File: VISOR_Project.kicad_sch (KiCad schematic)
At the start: 28 parts, among them U1 OPA170AIDBVR, U3 DRV8871DDA, U4 GD32VF103R, U5 MCP6002-xP, U6 MCP6002-xP

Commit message: project name
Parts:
- removed C5, C7: 100uF Keramisk, symbol Device:C_Small
- removed C6, C8: C_Polarized 4.7uF, symbol Device:C_Polarized
- removed NT1: NetTie_2, symbol Device:NetTie_2
- removed R10: 100Ω, symbol Device:R
- removed R7: 10kΩ, symbol Device:R
- removed R8: 5.1kΩ, symbol Device:R
- removed U5: MCP6002-xP, symbol Amplifier_Operational:MCP6002-xP
- removed unit 3 of U6
- added C1: 0.1uF, symbol Device:C
- added C2: 1uF, symbol Device:C
- added LD1: PL520, OptoDevice:LaserDiode_TO38ICut-3, symbol Diode_Laser:PL520
- added R1: 65Ω, symbol Device:R
- added R2: 390Ω, symbol Device:R
- added U2: LM317_TO-220, Package_TO_SOT_THT:TO-220-3_Vertical, symbol Regulator_Linear:LM317_TO-220
- added V1: 12, symbol Simulation_SPICE:VDC
- renumbered Ci to Ci1, R(SH) to R(SH)1
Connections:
- net at Ci1.1, R(SH)1.2: now also D1.2 (A); no longer D1.1 (K)
- net at C1.1, Ci1.2, R(SH)1.1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: now also D1.1 (K); no longer D1.2 (A)
- new net: C2.2, LD1.1 (A), R1.2, U2.2 (VO)
- new net: C1.1, C2.1, LD1.3 (C), R2.1, V1.2
- new net: C1.2, U2.3 (VI), V1.1
- new net: R1.1, R2.2, U2.1 (ADJ)
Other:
- moved on the sheet: D1, R5, R6

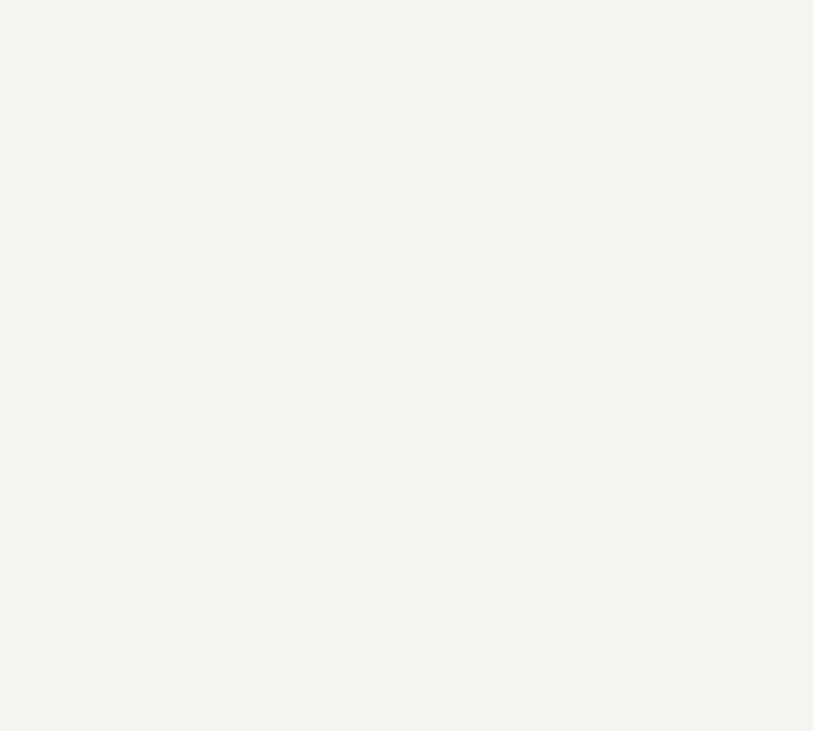
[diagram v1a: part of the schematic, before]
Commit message: Laser comonent added
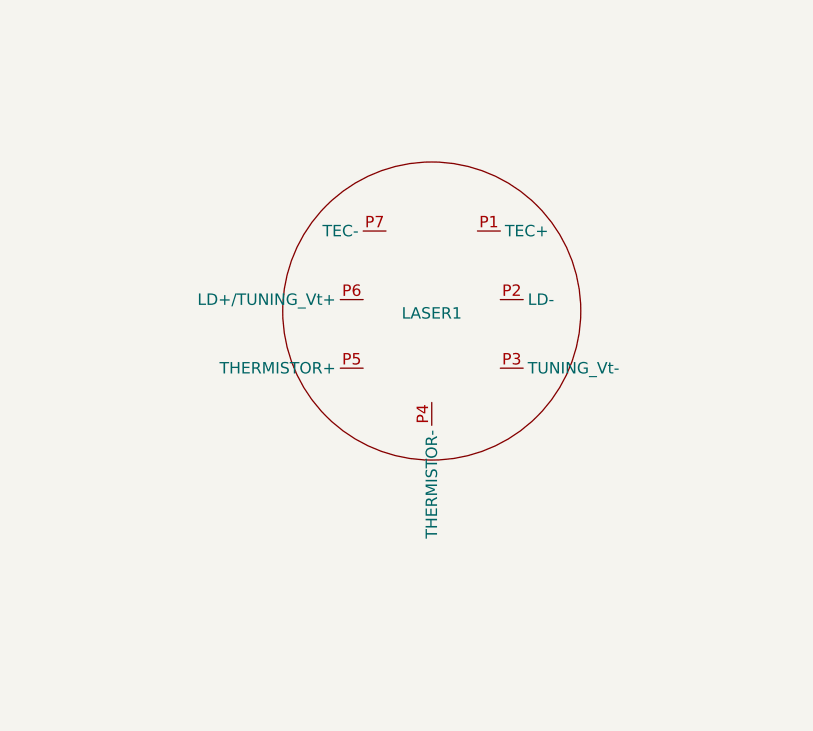
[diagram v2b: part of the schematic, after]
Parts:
- added LASER1: ~, symbol New_Library_0:7Pin_Socket_Laser
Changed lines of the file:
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@@
+	)
+	(symbol
+		(lib_id "New_Library_0:7Pin_Socket_Laser")
+		(at 306.07 184.15 0)
+		(unit 1)
+		(exclude_from_sim no)
+		(in_bom yes)
+		(on_board yes)
+		(dnp no)
+		(property "Reference" "LASER1"
+			(at 306.07 184.404 0)
+			(effects
+				(font
+					(size 1.27 1.27)
+				)
+			)
+		)
+		(property "Value" "~"
+			(at 306.07 204.47 0)
+			(effects
+				(font
+					(size 1.27 1.27)
+				)
+			)
+		)
+		(property "Footprint" ""
+			(at 306.07 184.15 0)
+			(effects
+				(font
+					(size 1.27 1.27)
+				)
+				(hide yes)
+			)
+		)
+		(property "Datasheet" "https://www.bandwidth10.com/wp-content/uploads/2025/05/BW10-1550-Txx-PxFA-C100-V2.4.pdf"
+			(at 306.07 184.15 0)
+			(effects
+				(font
+					(size 1.27 1.27)
+				)
+				(hide yes)
+			)
+		)
+		(property "Description" ""
+			(at 306.07 184.15 0)
+			(effects
+				(font
+					(size 1.27 1.27)
+				)
+				(hide yes)
+			)
+		)
+		(pin "P7"
+		)
+		(pin "P1"
+		)
+		(pin "P6"
+		)
+		(pin "P5"
+		)
+		(pin "P4"
+		)
+		(pin "P2"
+		)
+		(pin "P3"
+		)
+		(instances
+			(project ""
+				(path "/236c3ba3-cbc4-4020-b8ad-b2d57e4f816e"
+					(reference "LASER1")
+					(unit 1)
+				)
+			)
+		)
 	)
 	(symbol

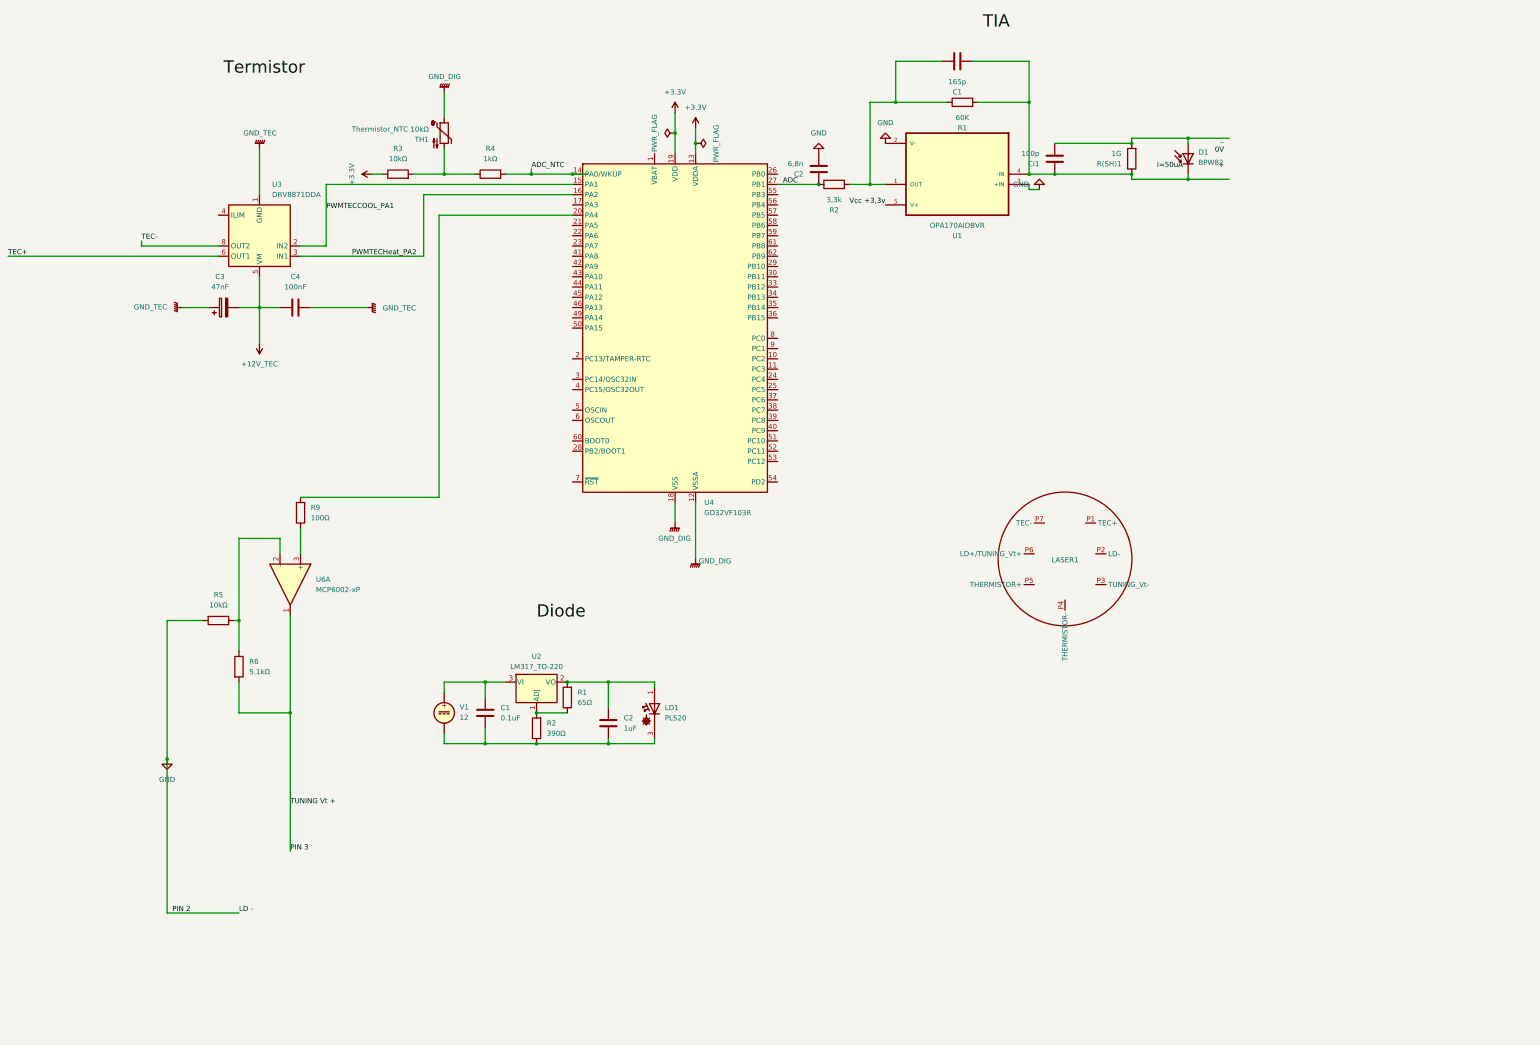
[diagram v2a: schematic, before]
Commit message: SPDT added
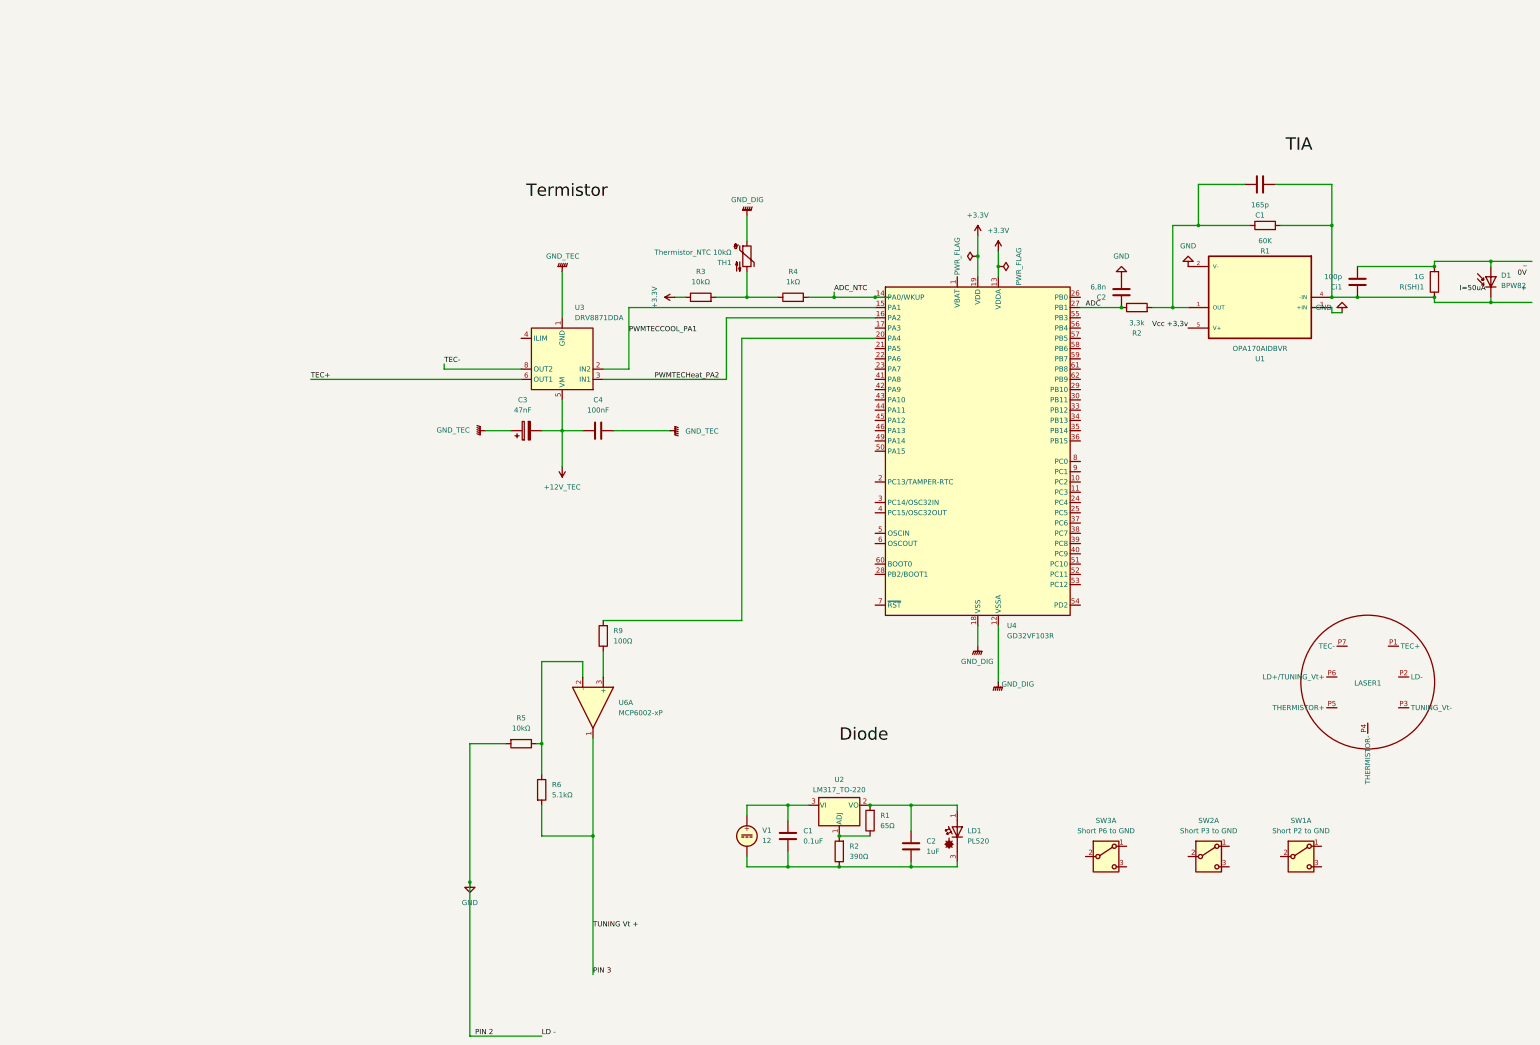
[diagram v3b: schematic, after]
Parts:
- added SW1: Short P2 to GND, symbol Switch:SW_DPDT_x2
- added SW2: Short P3 to GND, symbol Switch:SW_DPDT_x2
- added SW3: Short P6 to GND, symbol Switch:SW_DPDT_x2
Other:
- moved on the sheet: C1, C2, C3, C4, Ci1, D1, LASER1, LD1, R(SH)1, R1, R2, R3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

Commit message: test
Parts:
- removed Ci1: 100p, symbol Device:C
- removed R(SH)1: 1G, symbol Device:R
- removed R2: 390Ω, symbol Device:R
- added Ci: 0,6p, symbol Device:C
- added R_Extra: 0, symbol Device:R
- added U5: AD8676xR, Package_SO:SOIC-8_3.9x4.9mm_P1.27mm, symbol Amplifier_Operational:AD8676xR
- C1: value 165p -> 9.1p
- C2: value 6,8n -> ~
- R1: value 65Ω -> 42.5
- R1: value 60K -> 40.2K
- R2: value 3,3k -> ~
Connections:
- net GND: now also SW1.3 (C), SW2.3 (C), SW3.3 (C), U5.3 (+); no longer U1.2 (V-), U1.3 (+IN)
- net at C2.2, LD1.1 (A): now also R1.1, U2.1 (ADJ); no longer R1.2, U2.2 (VO)
- net at C1.1, D1.1 (K), R1.2: now also Ci.2, R_Extra.2, U5.2 (-); no longer U1.4 (-IN)
- net at D1.2 (A): now also Ci.1
- net at C1.2, R1.1, R2.2: now also R_Extra.1, U5.1; no longer U1.1 (OUT)
- net Vcc +3,3v: no longer names the net of U1.5 (V+)
- new net: R1.2, U2.2 (VO)
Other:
- moved on the sheet: C1, C2, D1, LASER1, R1, R2, U1
